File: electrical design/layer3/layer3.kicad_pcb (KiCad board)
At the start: 2 copper layers, 150 x 150 mm, 4 parts, among them J1 SH 1.0 6P, J2 SH 1.0 6P, J3 SH 1.0 6P, J4 SH 1.0 6P

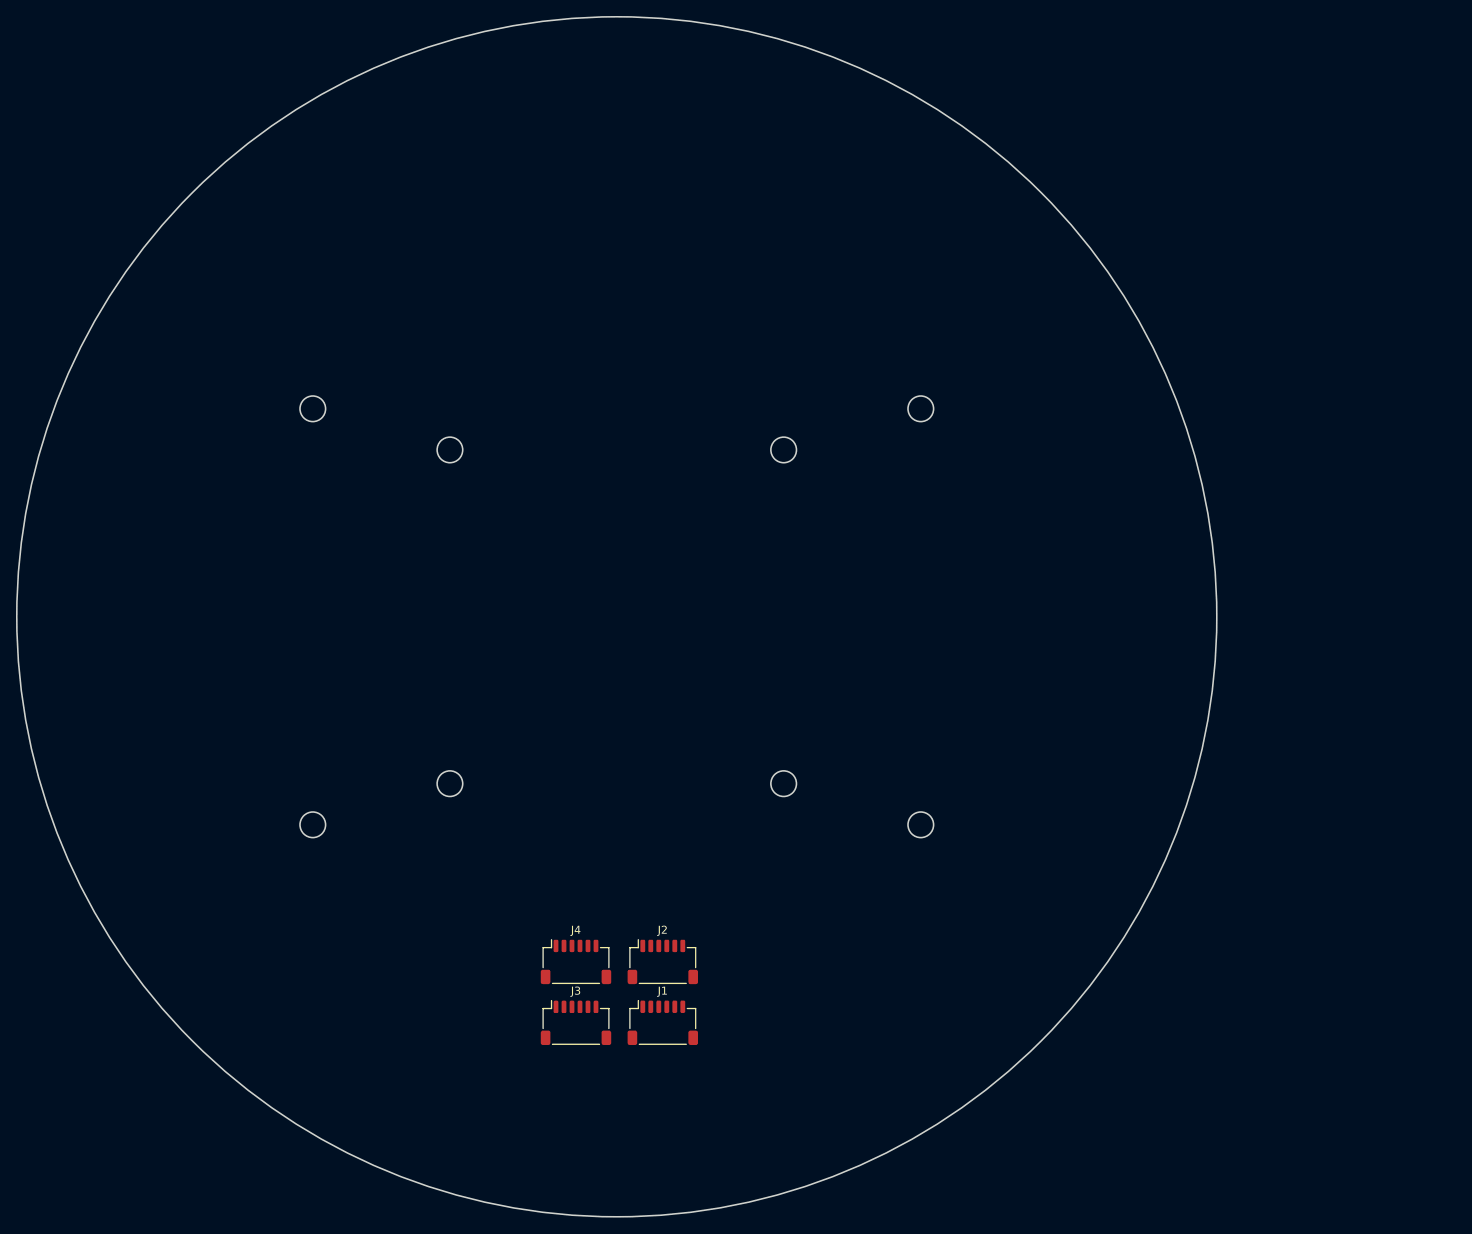
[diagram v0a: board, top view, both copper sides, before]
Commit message: lay out components on l3
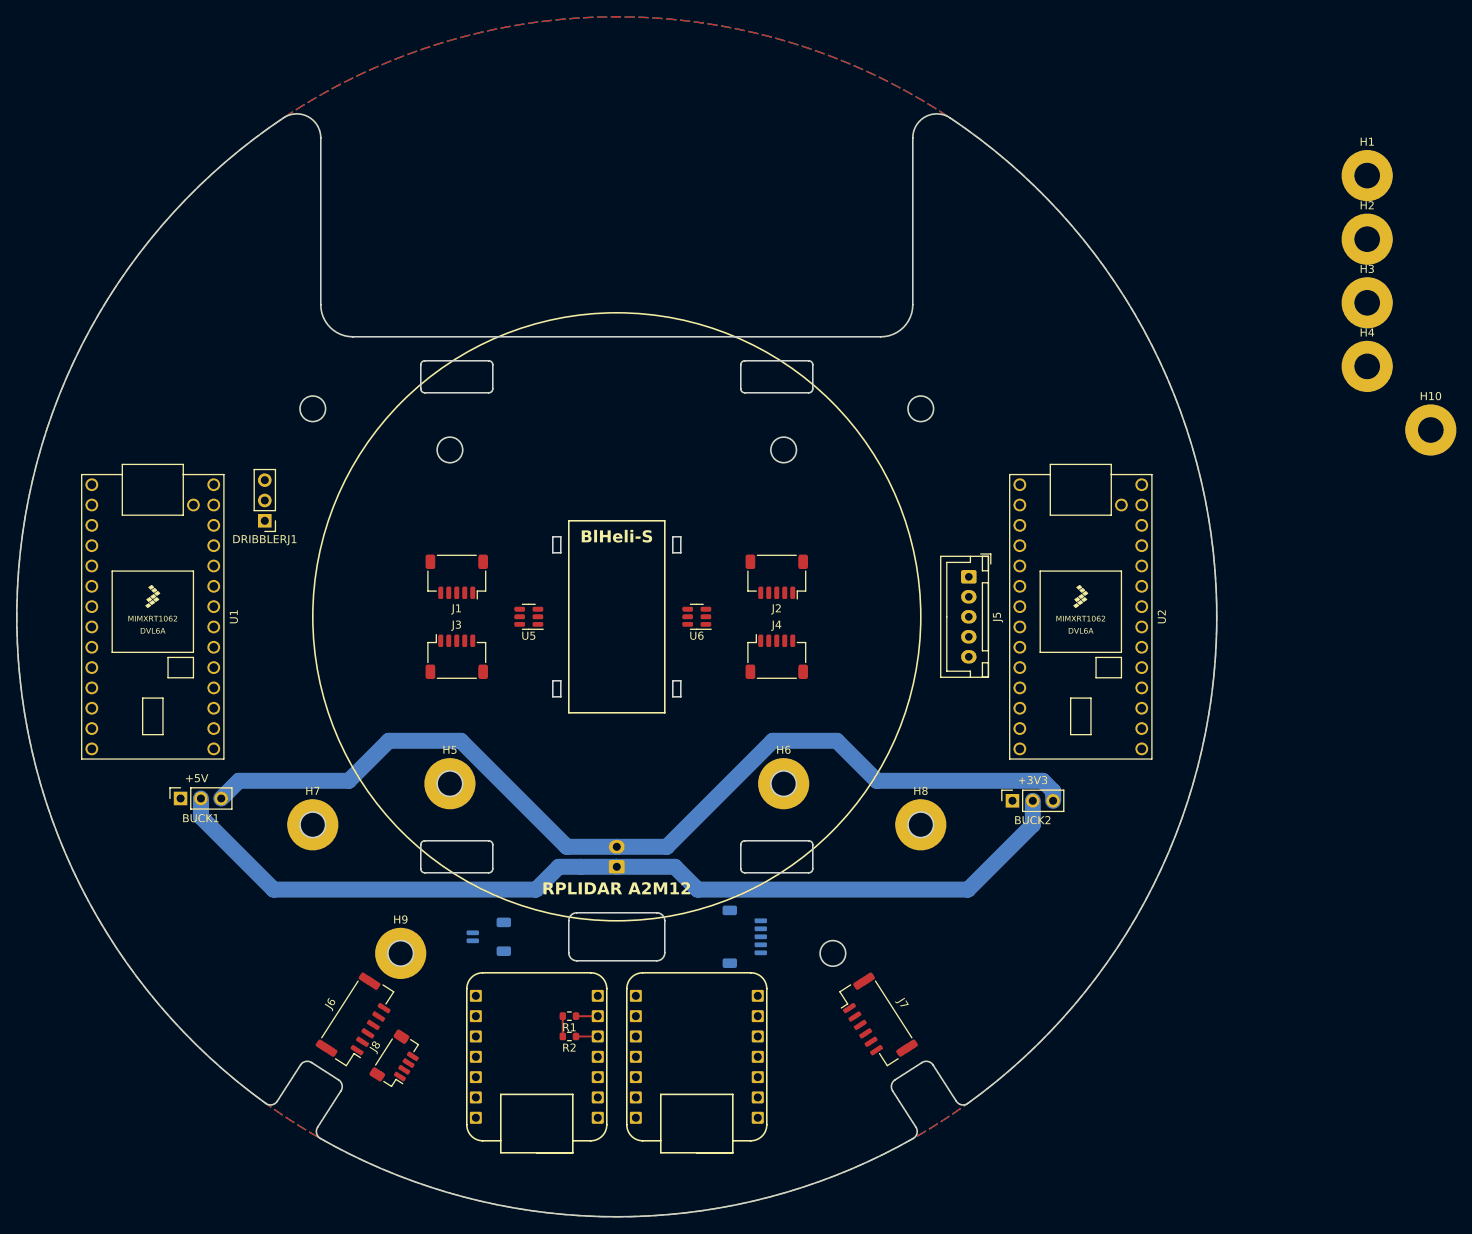
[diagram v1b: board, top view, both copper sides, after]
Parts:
- added BUCK1: +5V, Connector_PinSocket_2.54mm:PinSocket_1x03_P2.54mm_Vertical, F.Cu at (50.5, 127.7)
- added BUCK2: +3V3, Connector_PinSocket_2.54mm:PinSocket_1x03_P2.54mm_Vertical, F.Cu at (154.5, 128.0)
- added DRIBBLERJ1: Conn_01x03_Male, Connector_PinHeader_2.54mm:PinHeader_1x03_P2.54mm_Vertical, F.Cu at (61.0, 93.0)
- added H1: MountingHole, MountingHole:MountingHole_3.2mm_M3_Pad, F.Cu at (198.8, 49.9)
- added H10: MountingHole, MountingHole:MountingHole_3.2mm_M3_Pad, F.Cu at (206.8, 81.7)
- added H2: MountingHole, MountingHole:MountingHole_3.2mm_M3_Pad, F.Cu at (198.8, 57.8)
- added H3: MountingHole, MountingHole:MountingHole_3.2mm_M3_Pad, F.Cu at (198.8, 65.8)
- added H4: MountingHole, MountingHole:MountingHole_3.2mm_M3_Pad, F.Cu at (198.8, 73.7)
- added H5: MountingHole, MountingHole:MountingHole_3.2mm_M3_Pad, F.Cu at (84.1, 125.9)
- added H6: MountingHole, MountingHole:MountingHole_3.2mm_M3_Pad, F.Cu at (125.9, 125.9)
- added H7: MountingHole, MountingHole:MountingHole_3.2mm_M3_Pad, F.Cu at (67.0, 131.0)
- added H8: MountingHole, MountingHole:MountingHole_3.2mm_M3_Pad, F.Cu at (143.0, 131.0)
- added H9: MountingHole, MountingHole:MountingHole_3.2mm_M3_Pad, F.Cu at (78.0, 147.1)
- added J10: SH1.0 2P, Connector_JST:JST_SH_SM02B-SRSS-TB_1x02-1MP_P1.00mm_Horizontal, B.Cu at (89.0, 145.0)
- added J11: LAYER1, Connector_JST:JST_SH_SM05B-SRSS-TB_1x05-1MP_P1.00mm_Horizontal, B.Cu at (121.0, 145.0)
- added J5: XH2.54 5P, Connector_JST:JST_XH_B5B-XH-A_1x05_P2.50mm_Vertical, F.Cu at (149.0, 100.0)
- added J6: CAMERA1, Connector_JST:JST_GH_BM06B-GHS-TBT_1x06-1MP_P1.25mm_Vertical, F.Cu at (72.6, 155.5)
- added J7: CAMERA2, Connector_JST:JST_GH_BM06B-GHS-TBT_1x06-1MP_P1.25mm_Vertical, F.Cu at (137.4, 155.5)
- added J8: COMPASS, Connector_JST:JST_SH_BM04B-SRSS-TB_1x04-1MP_P1.00mm_Vertical, F.Cu at (77.6, 160.5)
- added J9: Conn_01x02_Pin, Connector_JST:JST_XH_B2B-XH-A_1x02_P2.50mm_Vertical, B.Cu at (105.0, 136.2)
- added R1: R, Resistor_SMD:R_0603_1608Metric, F.Cu at (99.1, 154.9)
- added R2: R, Resistor_SMD:R_0603_1608Metric, F.Cu at (99.1, 157.5)
- added U1: TEENSY 4.0, teensy:Teensy40, F.Cu at (47.0, 105.0)
- added U2: TEENSY 4.0, teensy:Teensy40, F.Cu at (163.0, 105.0)
- added U3: MOUDLE-SEEEDUINO-XIAO-ESP32C3, libraries:xiao-esp32c3, F.Cu at (95.0, 160.0)
- added U4: MOUDLE-SEEEDUINO-XIAO-ESP32C3, libraries:xiao-esp32c3, F.Cu at (115.0, 160.0)
- added U5: 74LVC2G04, Package_TO_SOT_SMD:SOT-23-6, F.Cu at (94.0, 105.0)
- added U6: 74LVC2G04, Package_TO_SOT_SMD:SOT-23-6, F.Cu at (115.0, 105.0)
- J1, J2, J3, J4: value SH 1.0 6P -> SH1.0 5P; footprint Connector_JST:JST_SH_SM06B-SRSS-TB_1x06-1MP_P1.00mm_Horizontal -> Connector_JST:JST_SH_SM05B-SRSS-TB_1x05-1MP_P1.00mm_Horizontal
- moved J1 61.4 mm to (85.0, 100.0), turned to 180 degrees
- moved J2 50.2 mm to (125.0, 100.0), turned to 180 degrees
- moved J3 48.1 mm to (85.0, 110.0)
- moved J4 45.7 mm to (125.0, 110.0)
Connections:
- J1 pad 5: /M1CS_DIS -> /M1INA
- J2 pad 5: /M2CS_DIS -> unconnected-(J2-Pin_5-Pad5)
- J3 pad 5: /M3CS_DIS -> /M3INA
- J4 pad 5: /M4CS_DIS -> /M4INA
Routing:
- net +12V: track 0.00 -> 121.8 mm
- net GNDPWR: track 0.00 -> 118.8 mm
- net /IMUSDA: track 0.00 -> 2.72 mm
- net /IMUSCL: track 0.00 -> 2.72 mm
- net Net-(J8-Pin_1): track 0.00 -> 2.54 mm
- added copper zone on B.Cu, net GNDD
- added copper zone on F.Cu, net GNDD
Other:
- board size 150 x 150 mm -> 150 x 137.9 mm
- board text added: "BlHeli-S"
- board text added: "RPLIDAR A2M12"
- board text added: "copyright © 2023. all rights reserved."
- board text added: "ducc."

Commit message: update pcbs and mech drawings
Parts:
- added SW1: SW_DPDT_x2, Switches:SWITCH_SPDT_PTH_11.6X4.0MM_LOCK, F.Cu at (62.0, 105.0)
- BUCK2: value +3V3 -> +5V
- moved H1 135.0 mm to (67.0, 79.0)
- moved H3 116.1 mm to (84.1, 84.1)
- moved H10 99.3 mm to (132.0, 147.1)
- moved H4 73.7 mm to (125.9, 84.1)
- moved H2 59.7 mm to (143.0, 79.0)
- turned U5 to 0 degrees
- turned U6 to 0 degrees
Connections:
- BUCK2 pad 1: +3V3 -> +5V
- J1 pad 2: /M1EN -> /EN
- J2 pad 2: /M2EN -> /EN
- J2 pad 5: unconnected-(J2-Pin_5-Pad5) -> /M2INA
- J3 pad 2: /M3EN -> /EN
- J4 pad 2: /M4EN -> /EN
- J6 pad 5: +5V -> unconnected-(J6-Pin_5-Pad5)
- J6 pad 6: GND -> unconnected-(J6-Pin_6-Pad6)
- J7 pad 5: +5V -> unconnected-(J7-Pin_5-Pad5)
- J7 pad 6: GND -> unconnected-(J7-Pin_6-Pad6)
- J8 pad 1: GND -> GNDD
- U1 pad 16: unconnected-(U1-Pad16) -> /M1CS
- U1 pad 17: unconnected-(U1-Pad17) -> /M2CS
- U1 pad 18: unconnected-(U1-Pad18) -> /M3CS
- U1 pad 19: unconnected-(U1-Pad19) -> /M4CS
- U5 pad 1: /M3INA -> /M1INA
- U5 pad 3: /M1INA -> /M3INA
- U5 pad 4: /M1INB -> /M3INB
- U5 pad 6: /M3INB -> /M1INB
- U6 pad 1: /M4INA -> /M2INA
- U6 pad 3: /M2INA -> /M4INA
- U6 pad 4: /M2INB -> /M4INB
- U6 pad 6: /M4INB -> /M2INB
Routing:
- net +5V: track 0.00 -> 317.1 mm, vias 0 -> 1
- net +3V3: track 0.00 -> 246.2 mm
- net /M2INB: track 0.00 -> 12.2 mm
- net /M1INA: track 0.00 -> 11.2 mm
- net /M1INB: track 0.00 -> 8.99 mm
- net /M4INB: track 0.00 -> 7.71 mm
- net /M4INA: track 0.00 -> 1.09 mm, vias 0 -> 1
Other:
- outline, holes or cut-outs redrawn

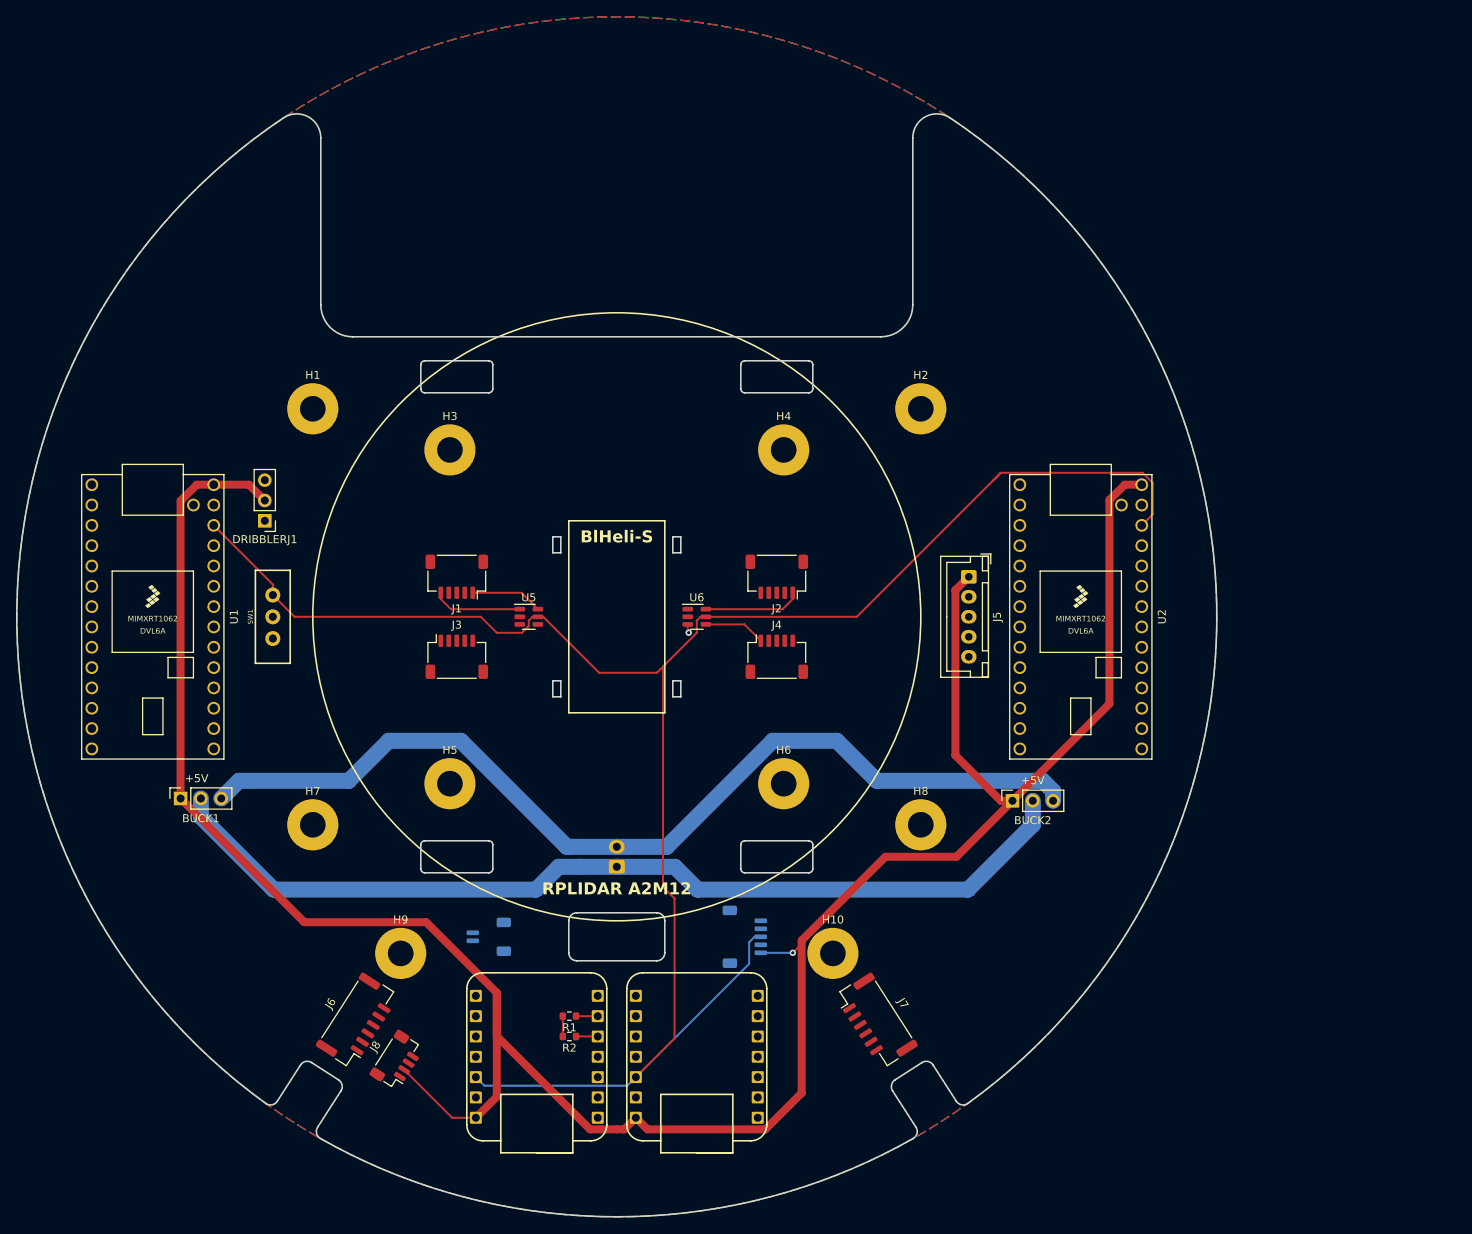
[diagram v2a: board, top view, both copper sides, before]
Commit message: routed layer 3
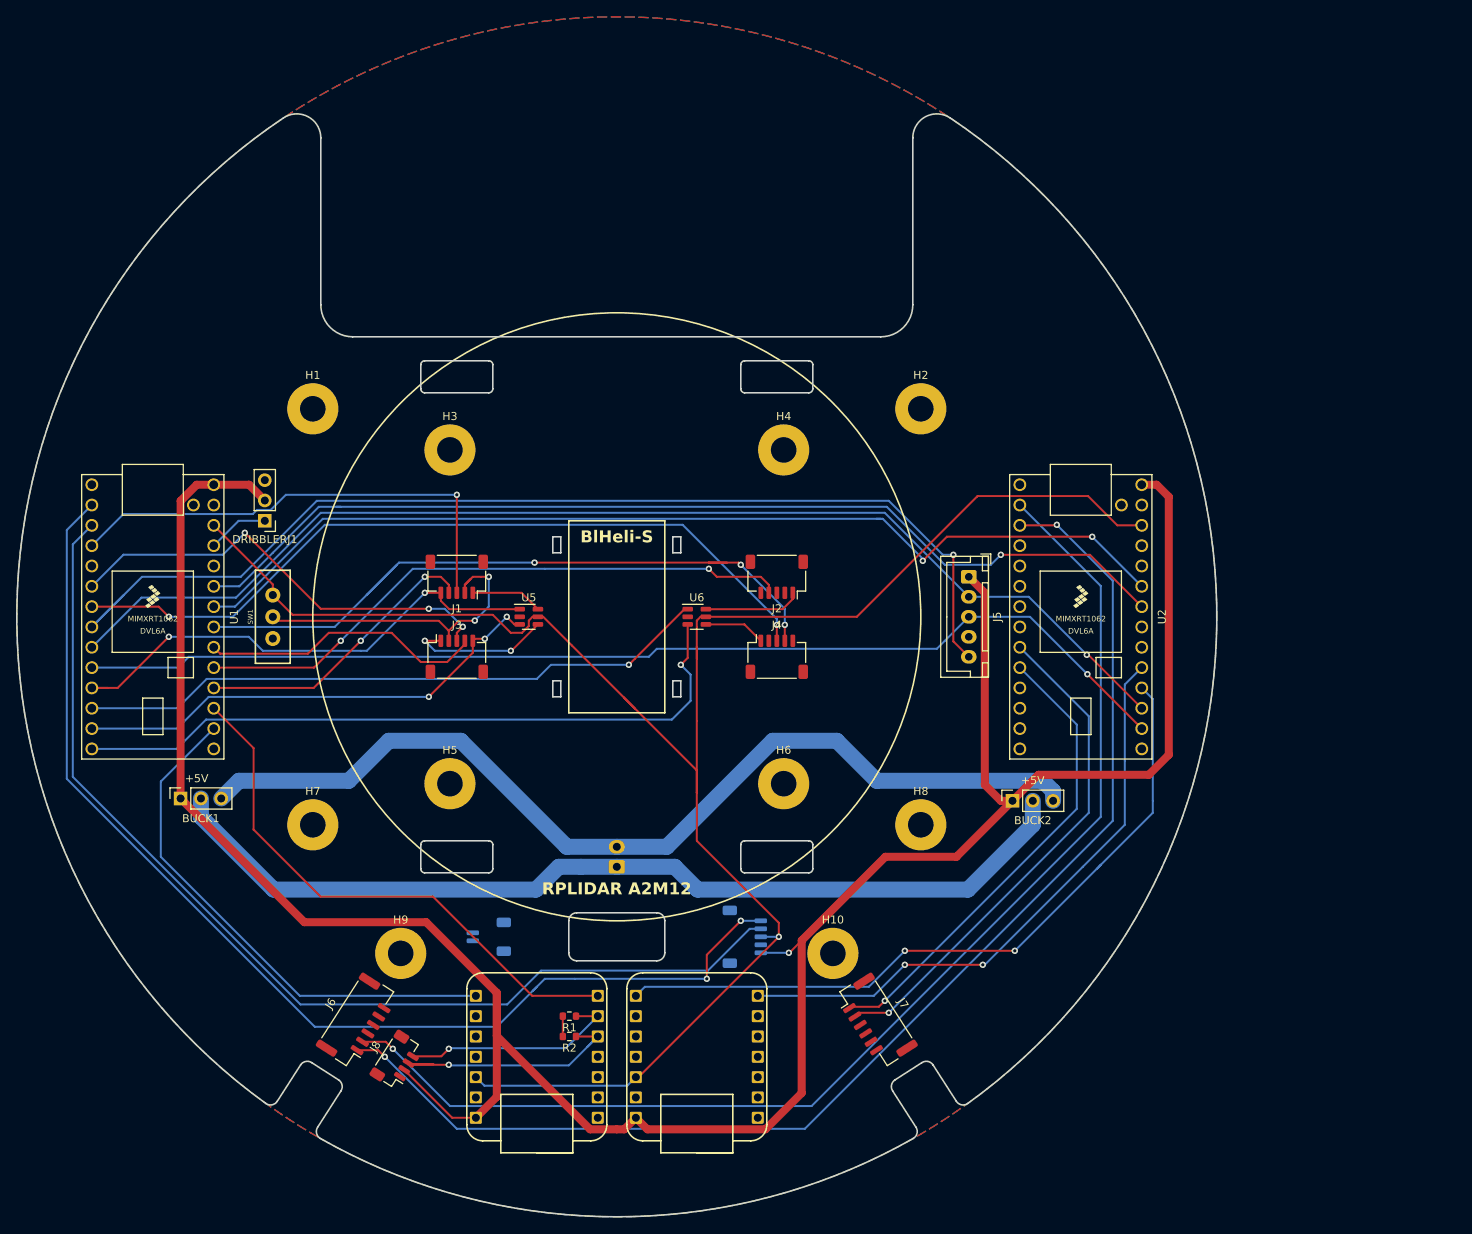
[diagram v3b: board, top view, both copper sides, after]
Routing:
- net /CAM1RX: track 0.00 -> 159.0 mm, vias 0 -> 2
- net /CAM1TX: track 0.00 -> 153.9 mm, vias 0 -> 1
- net /LIDARTX: track 0.00 -> 148.3 mm, vias 0 -> 1
- net /L1TX: track 0.00 -> 143.2 mm, vias 0 -> 2
- net /LIDARRX: track 0.00 -> 139.7 mm, vias 0 -> 1
- net /LIDARPWM: track 0.00 -> 136.2 mm, vias 0 -> 1
- net /L1RX: track 0.00 -> 134.1 mm
- net /RX: track 0.00 -> 127.2 mm, vias 0 -> 2
- net /TX: track 0.00 -> 126.8 mm, vias 0 -> 1
- net /M4PWM: track 0.00 -> 98.5 mm, vias 0 -> 2
- net /BTTX: track 0.00 -> 91.0 mm, vias 0 -> 2
- net /M4CS: track 0.00 -> 88.7 mm, vias 0 -> 3
- net /M4INA: track 1.09 -> 87.8 mm
- net /M2INA: track 0.00 -> 79.6 mm, vias 0 -> 1
- net /M2CS: track 0.00 -> 76.3 mm, vias 0 -> 2
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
